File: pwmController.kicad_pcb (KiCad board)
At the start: 2 copper layers, 100 x 100 mm, 67 parts, among them J1 track out, J10 RJ12, J11 Conn_01x06_Female, J12 gnd, J13 ADC, J15 ADC, J2 track out, J3 relays, J4 relays, J5 power, J6 inputs, J7 inputs, J8 Conn_01x06_Male, J9 RJ12, K1 G5V-1, K2 G5V-1, K3 G5V-1, K4 G5V-1, K5 G5V-1, K6 G5V-1, K7 G5V-1, K8 G5V-1, M1 Motor_Servo, M2 Motor_Servo, M3 Motor_Servo, M4 Motor_Servo, M5 Motor_Servo, M6 Motor_Servo, M7 Motor_Servo, M8 Motor_Servo, U1 L298N, U2 PCF8574, U3 ULN2803A, U4 MCP23017_SP, U5 MAX485E, U6 24LC256, U7 Buck

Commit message: redone the switch connectors to accomodate a current sense print. Rearranged parts and updated silk texts to be 50% of their original size
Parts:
- removed J12: gnd, TerminalBlock_Phoenix:TerminalBlock_Phoenix_MKDS-1,5-2-5.08_1x02_P5.08mm_Horizontal
- added J403: common, TerminalBlock_Phoenix:TerminalBlock_Phoenix_MPT-0,5-2-2.54_1x02_P2.54mm_Horizontal, F.Cu at (71.1, 71.4)
- moved C502 111.3 mm to (76.5, 103.4)
- moved C802 64.9 mm to (124.2, 31.2), turned to 0 degrees
- moved C801 63.5 mm to (131.8, 31.2), turned to 180 degrees
- moved C204 63.2 mm to (121.4, 58.9), turned to -90 degrees
- moved R201 32.3 mm to (81.0, 49.8), turned to 0 degrees
- moved C203 24.5 mm to (104.6, 56.7), turned to 90 degrees
- moved U301 18.9 mm to (117.2, 70.6)
- moved C201 16.6 mm to (104.6, 51.6), turned to 90 degrees
- moved D201 13.1 mm to (133.1, 52.8), turned to 180 degrees
- moved C301 12.2 mm to (121.4, 50.0), turned to 90 degrees
- moved D205 12.0 mm to (133.1, 48.3), turned to 180 degrees
- moved D206 11.7 mm to (125.5, 46.0), turned to 0 degrees
- moved D208 11.7 mm to (125.5, 55.1), turned to 0 degrees
- moved U201 10.00 mm to (109.2, 44.4), turned to -90 degrees
- moved U601 8.38 mm to (103.1, 80.8)
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- renumbered A1 to A901, C1 to C201, C2 to C202, C3 to C203, C4 to C204, C5 to C301, C6 to C501, C7 to C502, C8 to C601, C9 to C701, C10 to C801, C11 to C802, D1 to D201, D2 to D202, D3 to D203, D4 to D204, D5 to D205, D8 to D206, D9 to D207, D10 to D208, D6 to D501, D7 to D502, J1 to J201, J2 to J202, J3 to J301, J4 to J302, J6 to J401, J7 to J402, J5 to J501, J8 to J601, J9 to J602, J10 to J603, J11 to J604, J13 to J801, J15 to J802, JP1 to JP301, JP2 to JP302, K1 to K301, K2 to K302, K3 to K303, K4 to K304, K5 to K305, K6 to K306, K7 to K307, K8 to K308, M1 to M801, M2 to M802, M3 to M803, M4 to M804, M5 to M805, M6 to M806, M7 to M807, M8 to M808, R1 to R201, R2 to R202, U1 to U201, U2 to U301, U3 to U302, U4 to U401, U7 to U501, U5 to U601, U6 to U701

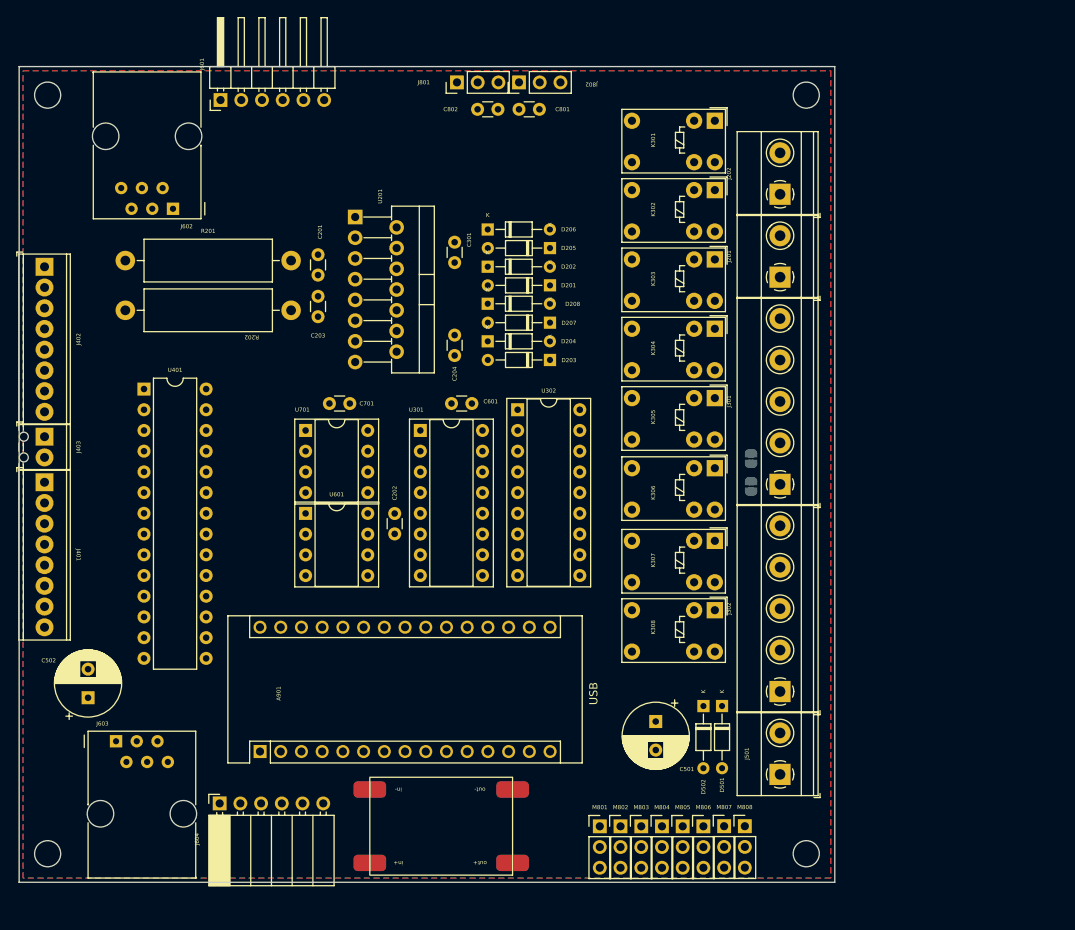
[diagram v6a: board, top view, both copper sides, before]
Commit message: I have a problem that I lose the links between symbols and footprints. I want to add a spst switch to connect the bus' voltage to the main power
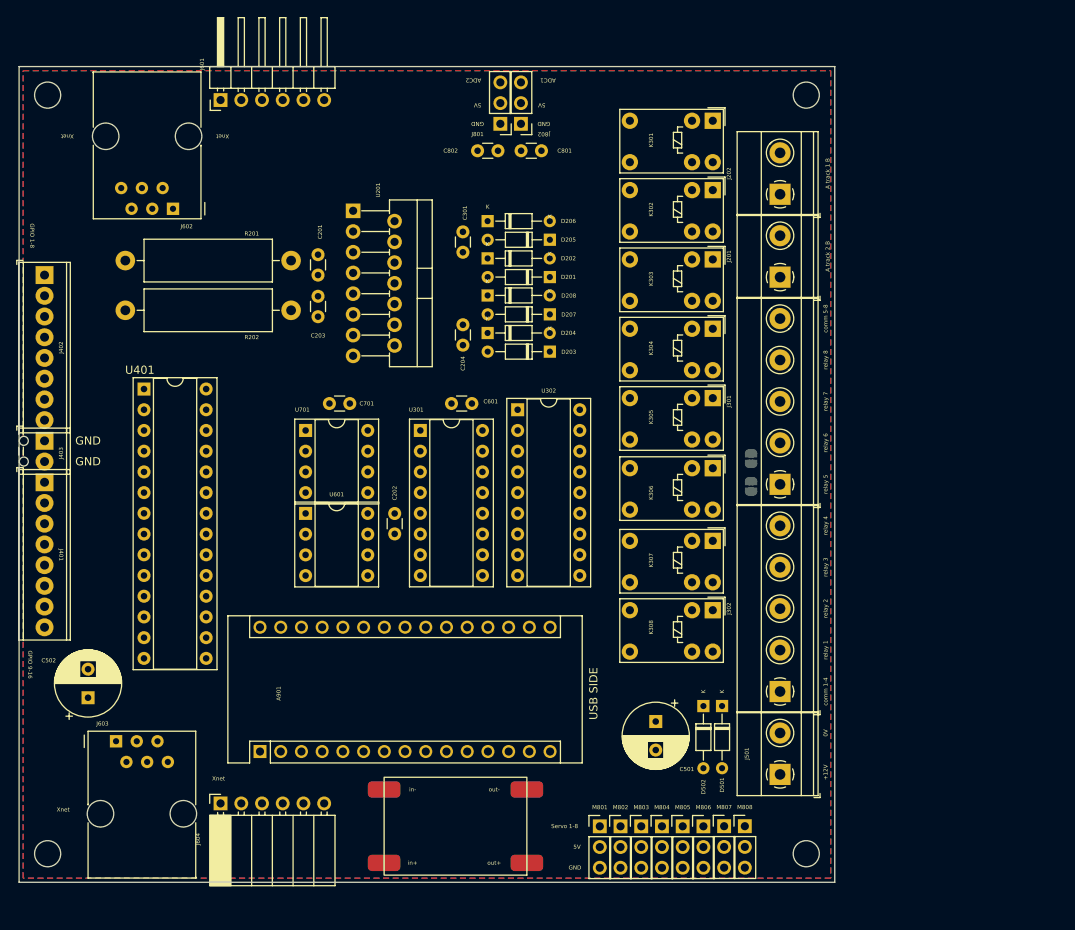
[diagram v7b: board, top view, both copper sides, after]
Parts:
- U401: footprint Package_DIP:DIP-28_W7.62mm -> Package_DIP:DIP-28_W7.62mm_Socket
- moved J801 7.36 mm to (127.0, 33.0), turned to 180 degrees
- moved C801 5.09 mm to (132.0, 36.3)
- moved J802 5.09 mm to (129.5, 33.0), turned to 180 degrees
- moved C802 5.08 mm to (124.2, 36.3)
- moved U501 1.75 mm to (123.8, 120.6)
- moved C204 1.63 mm to (122.4, 57.7)
- moved C301 1.63 mm to (122.4, 48.8)
- moved D201 1.02 mm to (133.1, 51.8)
- moved D204 1.02 mm to (125.4, 58.7)
- moved D205 1.02 mm to (133.1, 47.2)
- moved D206 1.02 mm to (125.4, 44.9)
- moved D207 1.02 mm to (133.1, 56.4)
- moved D208 1.02 mm to (125.4, 54.1)
- moved D202 1.02 mm to (125.4, 49.5)
- moved D203 1.02 mm to (133.1, 61.0)
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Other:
- board text added: "+12V"
- board text added: "0V"
- board text added: "5V"
- board text added: "A track 1 B"
- board text added: "A track 2 B"
- board text added: "ADC1"
- board text added: "ADC2"
- board text added: "GND"
- board text added: "GPIO 1-8"
- board text added: "GPIO 9-16"
- board text added: "Servo 1-8"
- board text added: "USB SIDE"
- board text added: "Xnet"
- board text added: "comm 1-4"
- board text added: "comm 5-8"
- board text added: "relay 1"
- board text added: "relay 2"
- board text added: "relay 3"
- board text added: "relay 4"
- board text added: "relay 5"
- board text added: "relay 6"
- board text added: "relay 7"
- board text added: "relay 8"
- board text removed: "USB"

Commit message: about to make new branch for control panel usage
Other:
- board text added: "A track1 B"
- board text added: "A track2 B"
- board text removed: "A track 1 B"
- board text removed: "A track 2 B"
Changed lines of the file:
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@@
     (effects (font (size 0.5 0.5) (thickness 0.075)))
   )
-  (gr_text "A track 2 B" (at 167.132 49.276 90) (layer "F.SilkS")
+  (gr_text "A track2 B" (at 167.132 49.276 90) (layer "F.SilkS")
     (effects (font (size 0.5 0.5) (thickness 0.075)))
   )
@@
     (effects (font (size 0.5 0.5) (thickness 0.075)))
   )
-  (gr_text "A track 1 B" (at 167.132 39.116 90) (layer "F.SilkS")
+  (gr_text "A track1 B" (at 167.132 39.116 90) (layer "F.SilkS")
     (effects (font (size 0.5 0.5) (thickness 0.075)))
   )
